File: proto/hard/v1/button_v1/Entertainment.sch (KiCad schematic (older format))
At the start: 46 parts, among them J6 Conn_01x08_Female, J8 AudioJack3, Q2 IRLML2060, Q4 IRLML2060, Q5 IRLML2060, Q8 TP0610T, U10 NL27WZ14, U5 RT9293, U8 ST485EBDR, U9 LM358

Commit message: Schematic libs clean-up
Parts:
- BZ1: footprint MyModules:buzz17 -> brbuttonsystem:buzz17; symbol MyModules:MyBuzzer -> brbuttonsystem:MyBuzzer
- J8: footprint MyConnectors:PJ-001-H -> brbuttonsystem:PJ-001-H
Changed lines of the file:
@@
 $EndComp
 $Comp
-L MyModules:MyBuzzer BZ?
+L brbuttonsystem:MyBuzzer BZ?
 U 1 1 5D318742
 P 3150 3350
@@
 F 0 "BZ1" V 3242 3378 50  0000 L CNN
 F 1 "MyBuzzer" V 3287 3378 50  0001 L CNN
-F 2 "MyModules:buzz17" H 3150 3350 50  0001 C CNN
+F 2 "brbuttonsystem:buzz17" H 3150 3350 50  0001 C CNN
 F 3 "" H 3150 3350 50  0001 C CNN
 	1    3150 3350
@@
 F 0 "J8" H 7050 1450 50  0000 C CNN
 F 1 "AudioJack3" H 7182 1484 50  0001 C CNN
-F 2 "MyConnectors:PJ-001-H" H 7200 1250 50  0001 C CNN
+F 2 "brbuttonsystem:PJ-001-H" H 7200 1250 50  0001 C CNN
 F 3 "~" H 7200 1250 50  0001 C CNN
 	1    7200 1250

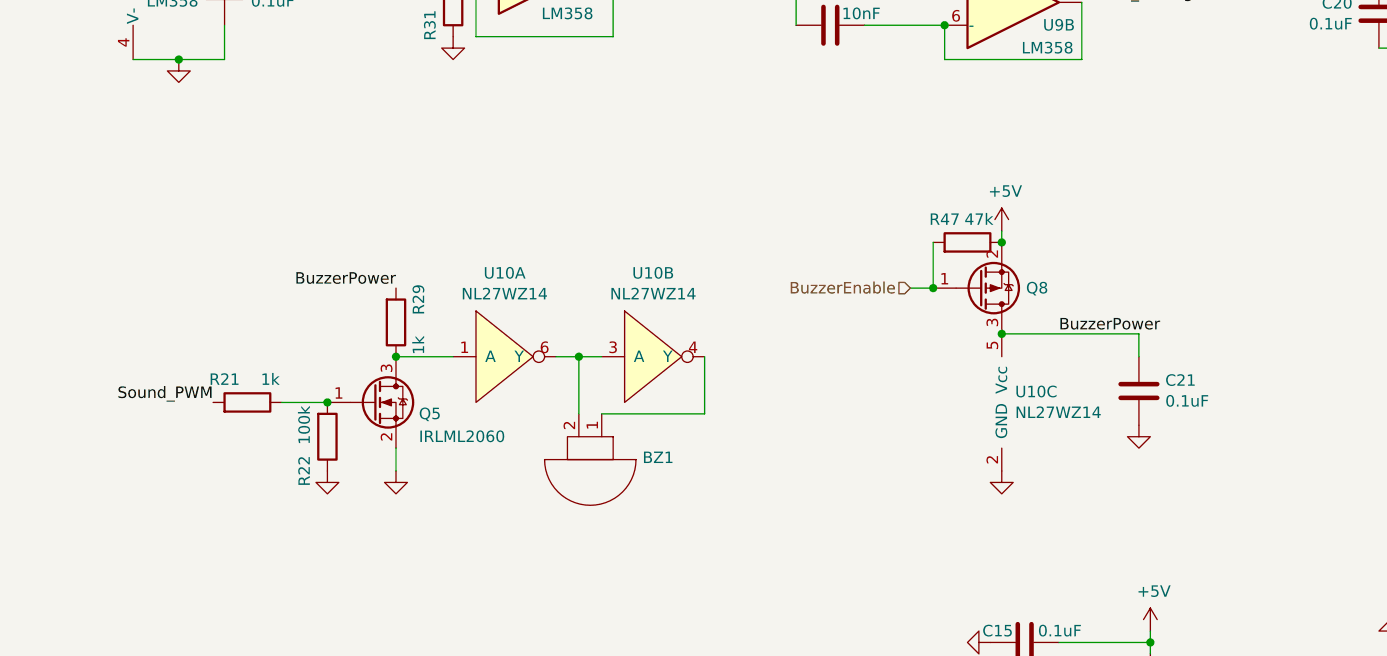
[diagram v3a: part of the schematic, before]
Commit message: Started schematic and PCB rework. Generated button_v1.pdf was left out of sync intentionally.
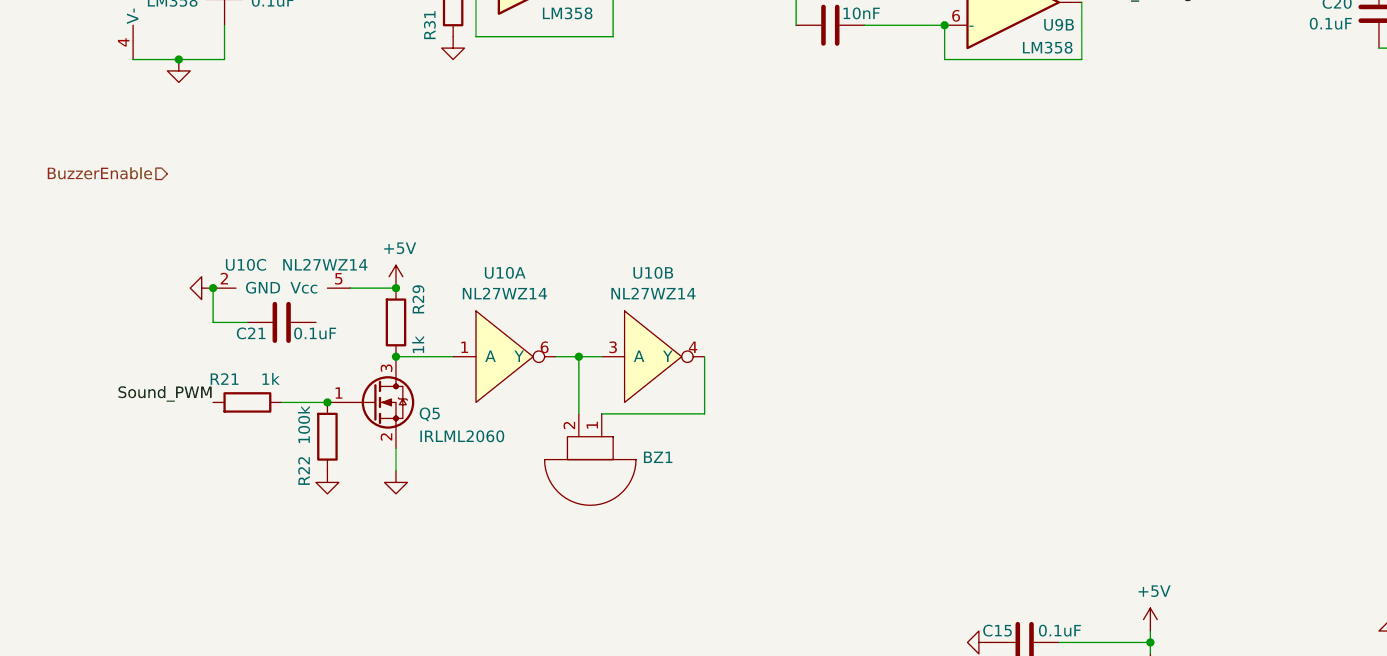
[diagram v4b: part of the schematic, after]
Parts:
- removed Q8: TP0610T, Package_TO_SOT_SMD:SOT-23, symbol Transistor_FET:TP0610T
- removed R47: 47k, Resistor_SMD:R_0805_2012Metric_Pad1.15x1.40mm_HandSolder, symbol Device:R
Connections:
- net +5V: now also R29.2, U10.5 (Vcc)
- removed net BuzzerPower: C21.1, R29.2, U10.5 (Vcc)
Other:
- moved on the sheet: C21, U10C
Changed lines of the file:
@@
 L brbuttonsystem:NL27WZ14 U?
 U 3 1 5D318716
-P 4750 2900
+P 1900 2700
 AR Path="/5D318716" Ref="U?"  Part="3"
 AR Path="/5D3754B9/5D318716" Ref="U10"  Part="3"
-F 0 "U10" H 4808 2646 50  0000 L CNN
-F 1 "NL27WZ14" H 4808 2555 50  0000 L CNN
-F 2 "Package_TO_SOT_SMD:SOT-23-6_Handsoldering" H 4750 2900 50  0001 C CNN
-F 3 "" H 4750 2900 50  0001 C CNN
-	3    4750 2900
-	1    0    0    -1
+F 0 "U10" V 1800 2150 50  0000 L CNN
+F 1 "NL27WZ14" V 1800 2400 50  0000 L CNN
+F 2 "Package_TO_SOT_SMD:SOT-23-6_Handsoldering" H 1900 2700 50  0001 C CNN
+F 3 "" H 1900 2700 50  0001 C CNN
+	3    1900 2700
+	0    1    1    0
 $EndComp
 Connection ~ 2100 3000
@@
 L power:+5V #PWR?
 U 1 1 5D31871F
-P 4750 2450
+P 2100 2700
 AR Path="/5D31871F" Ref="#PWR?"  Part="1"
 AR Path="/5D3754B9/5D31871F" Ref="#PWR061"  Part="1"
-F 0 "#PWR061" H 4750 2300 50  0001 C CNN
-F 1 "+5V" H 4765 2623 50  0000 C CNN
-F 2 "" H 4750 2450 50  0001 C CNN
-F 3 "" H 4750 2450 50  0001 C CNN
-	1    4750 2450
-	1    0    0    -1
-$EndComp
-$Comp
-L power:GND #PWR?
-U 1 1 5D318725
-P 4750 3500
-AR Path="/5D318725" Ref="#PWR?"  Part="1"
-AR Path="/5D3754B9/5D318725" Ref="#PWR062"  Part="1"
-F 0 "#PWR062" H 4750 3250 50  0001 C CNN
-F 1 "GND" H 4755 3327 50  0001 C CNN
-F 2 "" H 4750 3500 50  0001 C CNN
-F 3 "" H 4750 3500 50  0001 C CNN
-	1    4750 3500
+F 0 "#PWR061" H 2100 2550 50  0001 C CNN
+F 1 "+5V" H 2115 2873 50  0000 C CNN
+F 2 "" H 2100 2700 50  0001 C CNN
+F 3 "" H 2100 2700 50  0001 C CNN
+	1    2100 2700
 	1    0    0    -1
 $EndComp
@@
 L Device:C C?
 U 1 1 5D318730
-P 5350 3150
+P 1600 2850
 AR Path="/5D318730" Ref="C?"  Part="1"
 AR Path="/5D3754B9/5D318730" Ref="C21"  Part="1"
-F 0 "C21" H 5465 3196 50  0000 L CNN
-F 1 "0.1uF" H 5465 3105 50  0000 L CNN
-F 2 "Capacitor_SMD:C_0805_2012Metric_Pad1.15x1.40mm_HandSolder" H 5388 3000 50  0001 C CNN
-F 3 "~" H 5350 3150 50  0001 C CNN
-	1    5350 3150
-	1    0    0    -1
+F 0 "C21" V 1650 2650 50  0000 L CNN
+F 1 "0.1uF" V 1650 2900 50  0000 L CNN
+F 2 "Capacitor_SMD:C_0805_2012Metric_Pad1.15x1.40mm_HandSolder" H 1638 2700 50  0001 C CNN
+F 3 "~" H 1600 2850 50  0001 C CNN
+	1    1600 2850
+	0    1    1    0
 $EndComp
 $Comp
 L power:GND #PWR?
 U 1 1 5D31873C
-P 5350 3300
+P 1300 2700
 AR Path="/5D31873C" Ref="#PWR?"  Part="1"
 AR Path="/5D3754B9/5D31873C" Ref="#PWR064"  Part="1"
-F 0 "#PWR064" H 5350 3050 50  0001 C CNN
-F 1 "GND" H 5355 3127 50  0001 C CNN
-F 2 "" H 5350 3300 50  0001 C CNN
-F 3 "" H 5350 3300 50  0001 C CNN
-	1    5350 3300
-	1    0    0    -1
+F 0 "#PWR064" H 1300 2450 50  0001 C CNN
+F 1 "GND" H 1305 2527 50  0001 C CNN
+F 2 "" H 1300 2700 50  0001 C CNN
+F 3 "" H 1300 2700 50  0001 C CNN
+	1    1300 2700
+	0    1    1    0
 $EndComp
 $Comp
@@
 $EndComp
 $Comp
-L Transistor_FET:TP0610T Q?
-U 1 1 5D1677D4
-P 4650 2700
-AR Path="/5D1677D4" Ref="Q?"  Part="1"
-AR Path="/5D3754B9/5D1677D4" Ref="Q8"  Part="1"
-F 0 "Q8" H 4856 2700 50  0000 L CNN
-F 1 "TP0610T" H 4856 2655 50  0001 L CNN
-F 2 "Package_TO_SOT_SMD:SOT-23" H 4850 2625 50  0001 L CIN
-F 3 "http://www.vishay.com/docs/70209/70209.pdf" H 4650 2700 50  0001 L CNN
-	1    4650 2700
-	1    0    0    1
-$EndComp
-Wire Wire Line
-	4750 2900 5350 2900
-Wire Wire Line
-	5350 2900 5350 3000
-Connection ~ 4750 2900
-$Comp
-L Device:R R?
-U 1 1 5D192350
-P 4600 2500
-AR Path="/5D192350" Ref="R?"  Part="1"
-AR Path="/5D3754B9/5D192350" Ref="R47"  Part="1"
-F 0 "R47" V 4700 2400 50  0000 C CNN
-F 1 "47k" V 4700 2550 50  0000 C CNN
-F 2 "Resistor_SMD:R_0805_2012Metric_Pad1.15x1.40mm_HandSolder" V 4530 2500 50  0001 C CNN
-F 3 "~" H 4600 2500 50  0001 C CNN
-	1    4600 2500
-	0    1    -1   0
-$EndComp
-Wire Wire Line
-	4450 2700 4450 2500
-Wire Wire Line
-	4750 2450 4750 2500
-Connection ~ 4750 2500
-Text HLabel 4350 2700 0    50   Input ~ 0
-BuzzerEnable
-Wire Wire Line
-	4350 2700 4450 2700
-Connection ~ 4450 2700
-Text Label 5000 2900 0    50   ~ 0
-BuzzerPower
-Text Label 2100 2700 2    50   ~ 0
-BuzzerPower
-$Comp
 L Device:R R?
 U 1 1 5D16CC39
@@
 Wire Wire Line
 	4650 6550 4500 6550
+Text HLabel 1100 2200 0    50   Input ~ 0
+BuzzerEnable
+Wire Wire Line
+	2100 2700 1900 2700
+Connection ~ 2100 2700
+Wire Wire Line
+	1450 2850 1300 2850
+Wire Wire Line
+	1300 2850 1300 2700
+Connection ~ 1300 2700
 $EndSCHEMATC

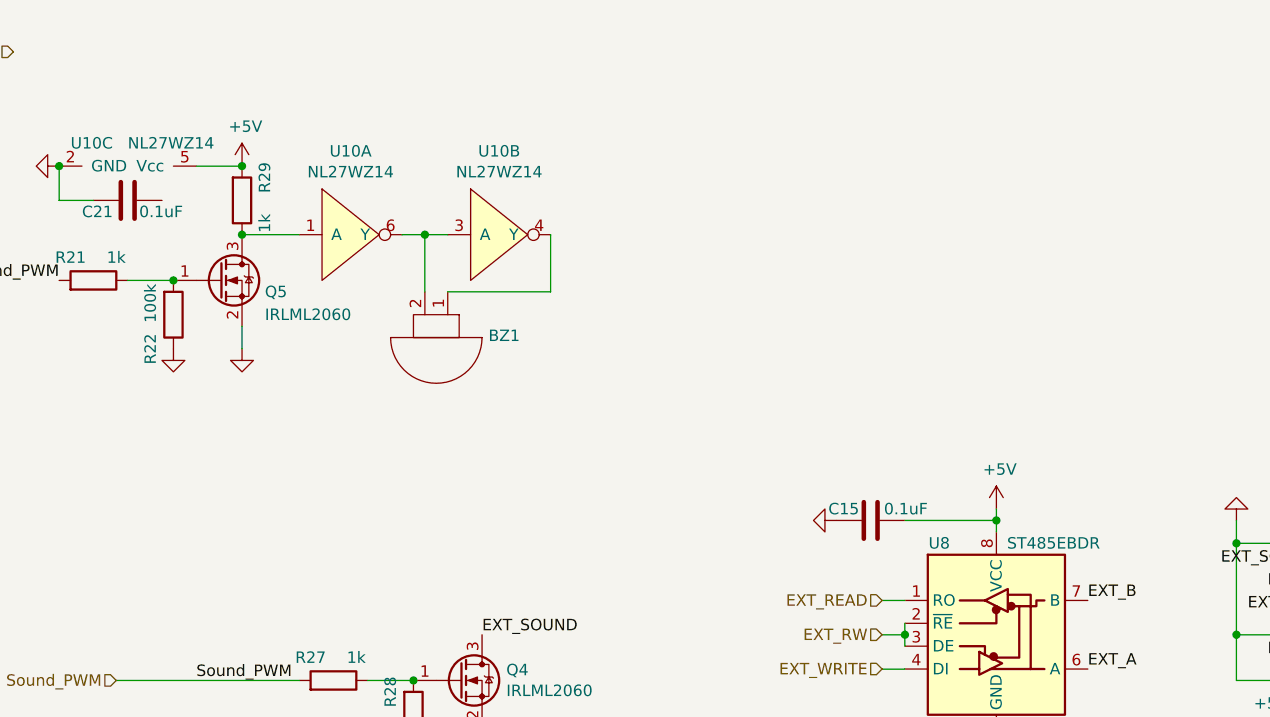
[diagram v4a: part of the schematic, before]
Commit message: PCB rework in progress. Centered main LCD. Added second LCD. Button connectors we shifted to the right.
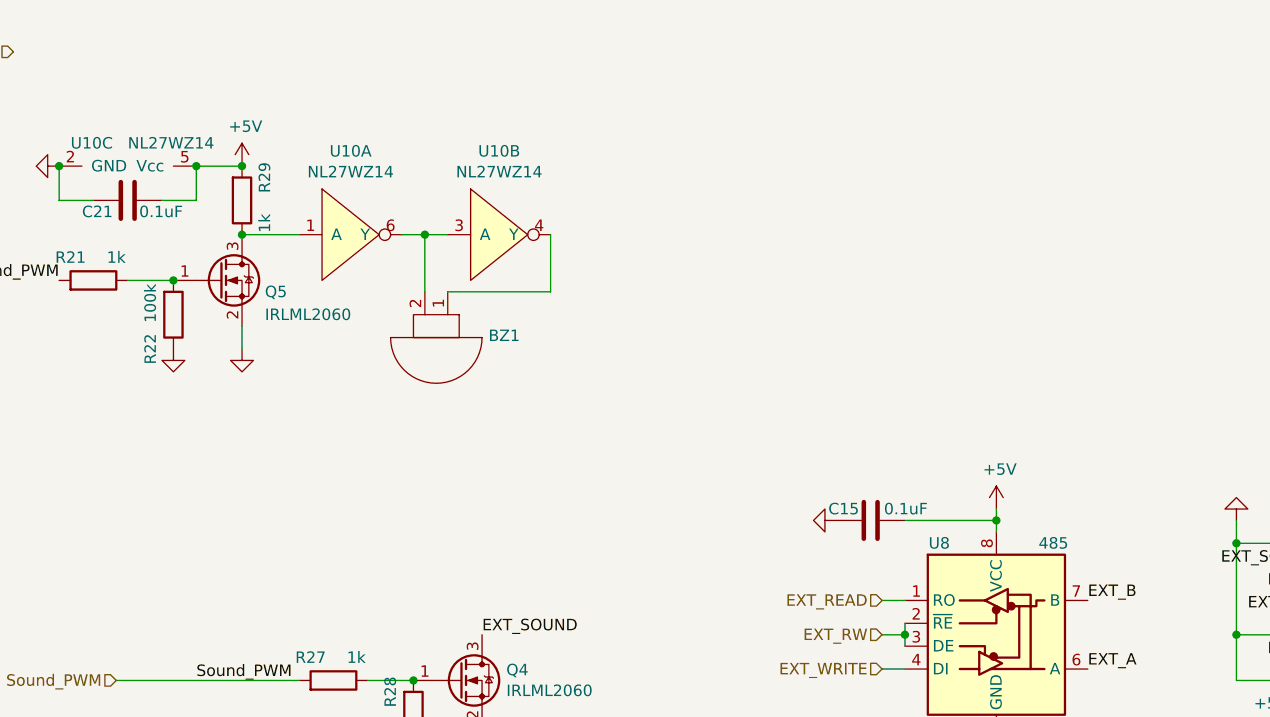
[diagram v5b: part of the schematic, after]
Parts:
- U8: value ST485EBDR -> 485
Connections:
- net +5V: now also C21.1
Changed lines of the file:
@@
 AR Path="/5D3754B9/5D1B415B" Ref="U8"  Part="1"
 F 0 "U8" H 5150 5050 50  0000 C CNN
-F 1 "ST485EBDR" H 5650 5050 50  0000 C CNN
+F 1 "485" H 5650 5050 50  0000 C CNN
 F 2 "Package_SO:SOIC-8_3.9x4.9mm_P1.27mm" H 5400 3800 50  0001 C CNN
 F 3 "http://www.st.com/resource/en/datasheet/st485eb.pdf" H 5400 4750 50  0001 C CNN
@@
 	1300 2850 1300 2700
 Connection ~ 1300 2700
+Wire Wire Line
+	1750 2850 1900 2850
+Wire Wire Line
+	1900 2850 1900 2700
+Connection ~ 1900 2700
 $EndSCHEMATC

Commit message: Updated main board to v0.3: - changed power coils to bobbin - added test point for StartLED line - integrated new LCD screen footprint with LED power connectors - changed Schottky diode footprint to smaller in start LED converter - changed crystal footprint to smaller - added guard ring around crystal - disconnected USB shield from GND line
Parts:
- D1: footprint Diode_SMD:D_SMA_Handsoldering -> Diode_SMD:D_SMA
- L2: footprint Inductor_SMD:L_0805_2012Metric_Pad1.15x1.40mm_HandSolder -> Inductor_SMD:L_Taiyo-Yuden_NR-50xx
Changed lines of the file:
@@
 F 0 "D1" H 5050 5850 50  0000 C CNN
 F 1 "STPS1L30A" H 5050 5825 50  0001 C CNN
-F 2 "Diode_SMD:D_SMA_Handsoldering" H 5050 5950 50  0001 C CNN
+F 2 "Diode_SMD:D_SMA" H 5050 5950 50  0001 C CNN
 F 3 "~" H 5050 5950 50  0001 C CNN
 	1    5050 5950
@@
 F 0 "L2" V 4500 6350 50  0000 C CNN
 F 1 "4.7uH" V 4500 6150 50  0000 C CNN
-F 2 "Inductor_SMD:L_0805_2012Metric_Pad1.15x1.40mm_HandSolder" H 4400 6250 50  0001 C CNN
+F 2 "Inductor_SMD:L_Taiyo-Yuden_NR-50xx" H 4400 6250 50  0001 C CNN
 F 3 "~" H 4400 6250 50  0001 C CNN
 	1    4400 6250
